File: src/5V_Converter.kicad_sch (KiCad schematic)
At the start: 13 parts, among them U3 TPS564257DRLR (12V-5V)

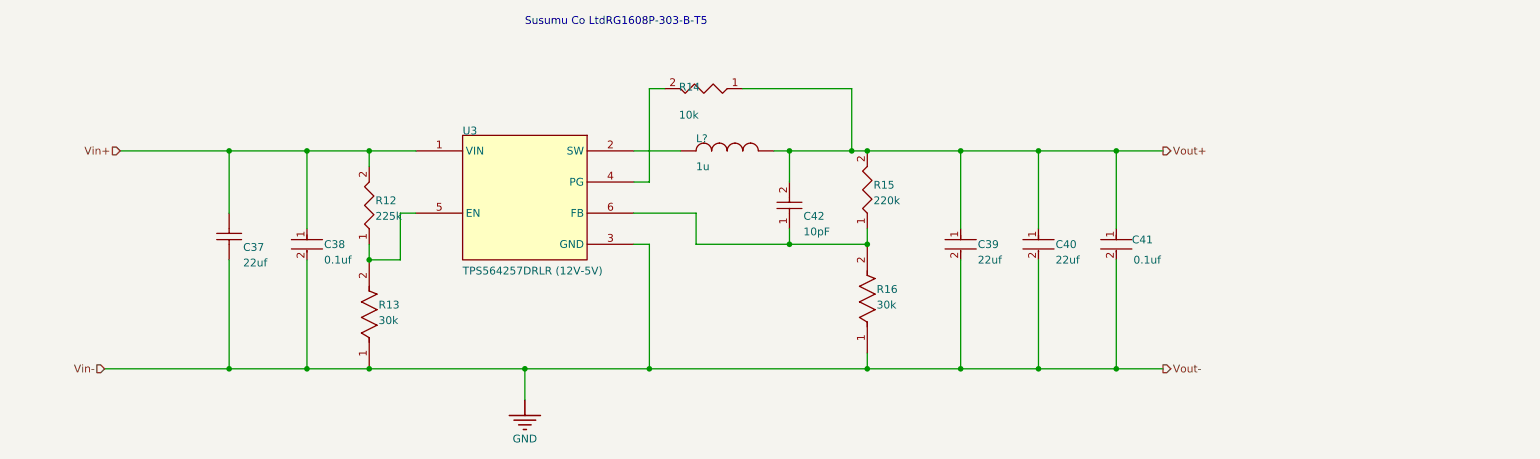
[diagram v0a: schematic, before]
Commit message: Updated majority of passive components to KiCad format
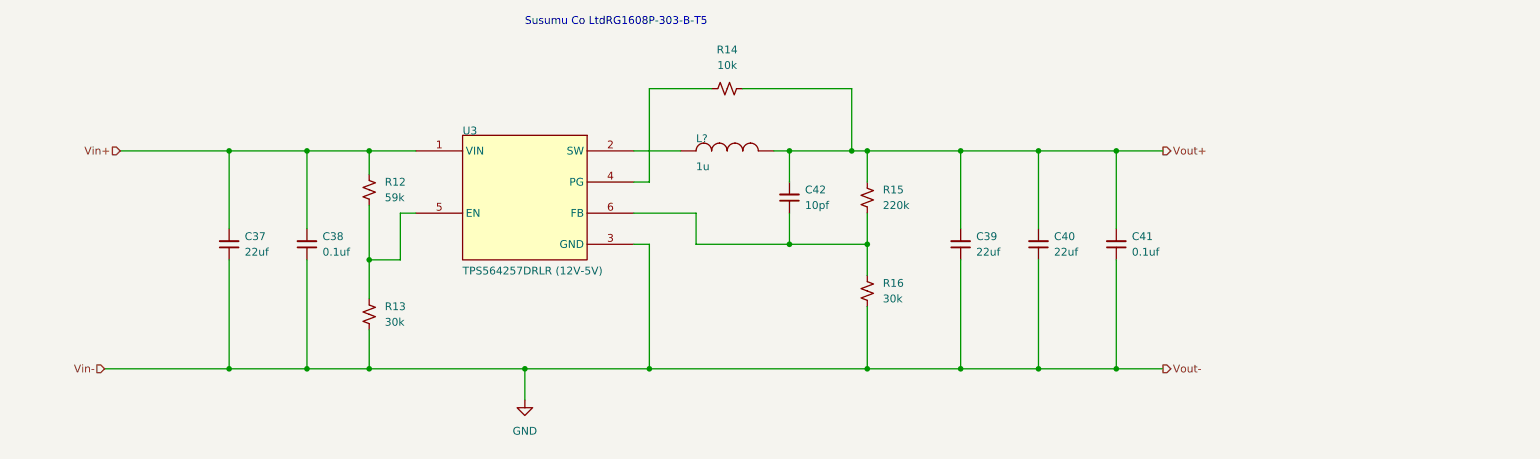
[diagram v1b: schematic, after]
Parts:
- removed C37: Capacitor, symbol Simulation Generic Components:Capacitor
- removed C38: 0.1uf, powerDristributionBoard-import-fps:FP-C0603C-CF-MFG, symbol Altium Content Vault:b4654b650e69147ec39a6b967a45e02
- removed C39, C40: 22uf, powerDristributionBoard-import-fps:FP-GRM21B-0_2-e0_2_0_7-IPC_C, symbol Altium Content Vault:b4654b650e69147ec39a6b967a45e02
- removed C41: 0.1uf, powerDristributionBoard-import-fps:FP-CGA3E-0_3-0_1-IPC_A, symbol Altium Content Vault:b4654b650e69147ec39a6b967a45e02
- removed C42: Capacitor 10 pF +/- 0.25 pF 50 V 0402, powerDristributionBoard-import-fps:CAPC1005X55X30LL05T10, symbol Autonomous Vehicle Lab:CAP-NP-2
- removed R12, R14, R15: 120R3J, powerDristributionBoard-import-fps:RESC0603(1608)_L, symbol Autonomous Vehicle Lab:120R3J
- removed R13, R16: 30k, powerDristributionBoard-import-fps:FP-RG1608-IPC_C, symbol Altium Content Vault:1029c3af85768c4190bb7ad29bc67b5
- added C37, C39, C40: 22uf, Capacitor_SMD:C_0805_2012Metric, symbol Device:C_Small
- added C38, C41: 0.1uf, Capacitor_SMD:C_0603_1608Metric, symbol Device:C_Small
- added C42: 10pf, Capacitor_SMD:C_0402_1005Metric, symbol Device:C_Small
- added R12: 59k, Resistor_SMD:R_0603_1608Metric, symbol Device:R_Small_US
- added R13, R16: 30k, Resistor_SMD:R_0603_1608Metric, symbol Device:R_Small_US
- added R14: 10k, Resistor_SMD:R_0603_1608Metric, symbol Device:R_Small_US
- added R15: 220k, Resistor_SMD:R_0603_1608Metric, symbol Device:R_Small_US
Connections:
- net GND: now also C37.1, C38.1, C39.1, C40.1, C41.1, R13.1, R16.1
- net Vin+: now also C37.2, C38.2, R12.2
- net Vout+: now also C39.2, C40.2, C41.2, C42.2, R14.2, R15.2
- net at U3.4 (PG): now also R14.1
- net at U3.5 (EN): now also R12.1, R13.2
- net at U3.6 (FB): now also C42.1, R15.1, R16.2

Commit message: Updated all passive components to KiCad version
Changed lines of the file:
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@@
 	(text "Susumu Co LtdRG1608P-303-B-T5"
 		(exclude_from_sim no)
-		(at 101.6 71.12 0)
+		(at 68.58 78.74 0)
 		(effects
 			(font

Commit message: Tweaked a lot stuff
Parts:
- gave numbers to parts that had none: 1
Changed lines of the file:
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@@
 		(instances
 			(project "powerDristributionBoard"
-				(path "/d5fc2ae9-f21d-48b0-bd61-912ade1f672f/f7fc7c23-3a4e-412b-b14d-71f85b15285a"
+				(path "/501e9f3f-9bfa-47dd-b56d-5fd6974f0d03/f7fc7c23-3a4e-412b-b14d-71f85b15285a"
 					(reference "R16")
 					(unit 1)
@@
 		(instances
 			(project "powerDristributionBoard"
-				(path "/d5fc2ae9-f21d-48b0-bd61-912ade1f672f/f7fc7c23-3a4e-412b-b14d-71f85b15285a"
+				(path "/501e9f3f-9bfa-47dd-b56d-5fd6974f0d03/f7fc7c23-3a4e-412b-b14d-71f85b15285a"
 					(reference "C37")
 					(unit 1)
@@
 		(instances
 			(project "powerDristributionBoard"
-				(path "/d5fc2ae9-f21d-48b0-bd61-912ade1f672f/f7fc7c23-3a4e-412b-b14d-71f85b15285a"
+				(path "/501e9f3f-9bfa-47dd-b56d-5fd6974f0d03/f7fc7c23-3a4e-412b-b14d-71f85b15285a"
 					(reference "#PWR016")
 					(unit 1)
@@
 		(instances
 			(project "powerDristributionBoard"
-				(path "/d5fc2ae9-f21d-48b0-bd61-912ade1f672f/f7fc7c23-3a4e-412b-b14d-71f85b15285a"
+				(path "/501e9f3f-9bfa-47dd-b56d-5fd6974f0d03/f7fc7c23-3a4e-412b-b14d-71f85b15285a"
 					(reference "U3")
 					(unit 1)
@@
 		(instances
 			(project "powerDristributionBoard"
-				(path "/d5fc2ae9-f21d-48b0-bd61-912ade1f672f/f7fc7c23-3a4e-412b-b14d-71f85b15285a"
+				(path "/501e9f3f-9bfa-47dd-b56d-5fd6974f0d03/f7fc7c23-3a4e-412b-b14d-71f85b15285a"
 					(reference "C41")
 					(unit 1)
@@
 		(instances
 			(project "powerDristributionBoard"
-				(path "/d5fc2ae9-f21d-48b0-bd61-912ade1f672f/f7fc7c23-3a4e-412b-b14d-71f85b15285a"
+				(path "/501e9f3f-9bfa-47dd-b56d-5fd6974f0d03/f7fc7c23-3a4e-412b-b14d-71f85b15285a"
 					(reference "R14")
 					(unit 1)
@@
 		(instances
 			(project "powerDristributionBoard"
-				(path "/d5fc2ae9-f21d-48b0-bd61-912ade1f672f/f7fc7c23-3a4e-412b-b14d-71f85b15285a"
+				(path "/501e9f3f-9bfa-47dd-b56d-5fd6974f0d03/f7fc7c23-3a4e-412b-b14d-71f85b15285a"
 					(reference "C40")
 					(unit 1)
@@
 		(instances
 			(project "powerDristributionBoard"
-				(path "/d5fc2ae9-f21d-48b0-bd61-912ade1f672f/f7fc7c23-3a4e-412b-b14d-71f85b15285a"
+				(path "/501e9f3f-9bfa-47dd-b56d-5fd6974f0d03/f7fc7c23-3a4e-412b-b14d-71f85b15285a"
 					(reference "C42")
 					(unit 1)
@@
 		(instances
 			(project "powerDristributionBoard"
-				(path "/d5fc2ae9-f21d-48b0-bd61-912ade1f672f/f7fc7c23-3a4e-412b-b14d-71f85b15285a"
+				(path "/501e9f3f-9bfa-47dd-b56d-5fd6974f0d03/f7fc7c23-3a4e-412b-b14d-71f85b15285a"
 					(reference "C39")
 					(unit 1)
@@
 		(instances
 			(project "powerDristributionBoard"
-				(path "/d5fc2ae9-f21d-48b0-bd61-912ade1f672f/f7fc7c23-3a4e-412b-b14d-71f85b15285a"
+				(path "/501e9f3f-9bfa-47dd-b56d-5fd6974f0d03/f7fc7c23-3a4e-412b-b14d-71f85b15285a"
 					(reference "R12")
 					(unit 1)
@@
 		(in_pos_files yes)
 		(dnp no)
-		(property "Reference" "L?"
+		(property "Reference" "L2"
 			(at 129.54 90.17 0)
 			(show_name no)
@@
 		(instances
 			(project "powerDristributionBoard"
-				(path "/d5fc2ae9-f21d-48b0-bd61-912ade1f672f/f7fc7c23-3a4e-412b-b14d-71f85b15285a"
-					(reference "L?")
+				(path "/501e9f3f-9bfa-47dd-b56d-5fd6974f0d03/f7fc7c23-3a4e-412b-b14d-71f85b15285a"
+					(reference "L2")
 					(unit 1)
 				)
@@
 		(instances
 			(project "powerDristributionBoard"
-				(path "/d5fc2ae9-f21d-48b0-bd61-912ade1f672f/f7fc7c23-3a4e-412b-b14d-71f85b15285a"
+				(path "/501e9f3f-9bfa-47dd-b56d-5fd6974f0d03/f7fc7c23-3a4e-412b-b14d-71f85b15285a"
 					(reference "R15")
 					(unit 1)
@@
 		(instances
 			(project "powerDristributionBoard"
-				(path "/d5fc2ae9-f21d-48b0-bd61-912ade1f672f/f7fc7c23-3a4e-412b-b14d-71f85b15285a"
+				(path "/501e9f3f-9bfa-47dd-b56d-5fd6974f0d03/f7fc7c23-3a4e-412b-b14d-71f85b15285a"
 					(reference "R13")
 					(unit 1)
@@
 		(instances
 			(project "powerDristributionBoard"
-				(path "/d5fc2ae9-f21d-48b0-bd61-912ade1f672f/f7fc7c23-3a4e-412b-b14d-71f85b15285a"
+				(path "/501e9f3f-9bfa-47dd-b56d-5fd6974f0d03/f7fc7c23-3a4e-412b-b14d-71f85b15285a"
 					(reference "C38")
 					(unit 1)

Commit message: Pushing remaining schematic files
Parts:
- removed L2: Inductor, symbol Simulation Generic Components:Inductor
- added L2: 1uH, symbol Device:L
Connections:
- net Vout+: now also L2.2
- net at U3.2 (SW): now also L2.1
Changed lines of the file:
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@@
 	(generator_version "10.0")
 	(paper "A")
+	(rectangle
+		(start 127 83.82)
+		(end 142.24 95.25)
+		(stroke
+			(width 0)
+			(type solid)
+			(color 255 7 0 1)
+		)
+		(fill
+			(type none)
+		)
+	)
 	(text "Susumu Co LtdRG1608P-303-B-T5"
 		(exclude_from_sim no)
@@
 	(wire
 		(pts
-			(xy 127 91.44) (xy 119.38 91.44)
+			(xy 119.38 91.44) (xy 130.81 91.44)
 		)
 		(stroke
@@
 	(wire
 		(pts
-			(xy 144.78 91.44) (xy 142.24 91.44)
-		)
-		(stroke
-			(width 0)
-			(type default)
-		)
-	)
-	(wire
-		(pts
 			(xy 154.94 91.44) (xy 144.78 91.44)
 		)
@@
 		(pts
 			(xy 144.78 96.52) (xy 144.78 91.44)
+		)
+		(stroke
+			(width 0)
+			(type default)
+		)
+	)
+	(wire
+		(pts
+			(xy 138.43 91.44) (xy 144.78 91.44)
 		)
 		(stroke
@@
 	)
 	(symbol
-		(lib_id "Simulation Generic Components:Inductor")
-		(at 127 91.44 0)
+		(lib_id "Device:L")
+		(at 134.62 91.44 90)
 		(unit 1)
 		(body_style 1)
@@
 		(in_pos_files yes)
 		(dnp no)
+		(fields_autoplaced yes)
 		(property "Reference" "L2"
-			(at 129.54 90.17 0)
-			(show_name no)
-			(do_not_autoplace no)
-			(effects
-				(font
-					(size 1.27 1.27)
-				)
-				(justify left bottom)
-			)
-		)
-		(property "Value" "Inductor"
-			(at 129.54 94.742 0)
-			(hide yes)
-			(show_name no)
-			(do_not_autoplace no)
-			(effects
-				(font
-					(size 1.27 1.27)
-				)
-				(justify left bottom)
+			(at 134.62 86.36 90)
+			(show_name no)
+			(do_not_autoplace no)
+			(effects
+				(font
+					(size 1.27 1.27)
+				)
+			)
+		)
+		(property "Value" "1uH"
+			(at 134.62 88.9 90)
+			(show_name no)
+			(do_not_autoplace no)
+			(effects
+				(font
+					(size 1.27 1.27)
+				)
 			)
 		)
 		(property "Footprint" ""
-			(at 127 91.44 0)
+			(at 134.62 91.44 0)
 			(hide yes)
 			(show_name no)
@@
 		)
 		(property "Datasheet" ""
-			(at 127 91.44 0)
+			(at 134.62 91.44 0)
 			(hide yes)
 			(show_name no)
@@
 		)
 		(property "Description" "Inductor"
-			(at 127 91.44 0)
-			(hide yes)
-			(show_name no)
-			(do_not_autoplace no)
-			(effects
-				(font
-					(size 1.27 1.27)
-				)
-			)
-		)
-		(property "SIMULATIONGENERICCOMPONENT" "True"
-			(at 129.54 97.282 0)
-			(hide yes)
-			(show_name no)
-			(do_not_autoplace no)
-			(effects
-				(font
-					(size 1.27 1.27)
-				)
-				(justify left bottom)
-			)
-		)
-		(property "DTEMP" ""
-			(at 142.748 92.202 0)
-			(hide yes)
-			(show_name no)
-			(do_not_autoplace no)
-			(effects
-				(font
-					(size 1.27 1.27)
-				)
-				(justify left bottom)
-			)
-		)
-		(property "T_REL_LOCAL" ""
-			(at 142.748 92.202 0)
-			(hide yes)
-			(show_name no)
-			(do_not_autoplace no)
-			(effects
-				(font
-					(size 1.27 1.27)
-				)
-				(justify left bottom)
-			)
-		)
-		(property "INITIAL CURRENT" ""
-			(at 142.748 92.202 0)
-			(hide yes)
-			(show_name no)
-			(do_not_autoplace no)
-			(effects
-				(font
-					(size 1.27 1.27)
-				)
-				(justify left bottom)
-			)
-		)
-		(property "CPAR" ""
-			(at 142.748 92.202 0)
-			(hide yes)
-			(show_name no)
-			(do_not_autoplace no)
-			(effects
-				(font
-					(size 1.27 1.27)
-				)
-				(justify left bottom)
-			)
-		)
-		(property "M" ""
-			(at 142.748 92.202 0)
-			(hide yes)
-			(show_name no)
-			(do_not_autoplace no)
-			(effects
-				(font
-					(size 1.27 1.27)
-				)
-				(justify left bottom)
-			)
-		)
-		(property "RPAR" ""
-			(at 142.748 92.202 0)
-			(hide yes)
-			(show_name no)
-			(do_not_autoplace no)
-			(effects
-				(font
-					(size 1.27 1.27)
-				)
-				(justify left bottom)
-			)
-		)
-		(property "RSER" ""
-			(at 142.748 92.202 0)
-			(hide yes)
-			(show_name no)
-			(do_not_autoplace no)
-			(effects
-				(font
-					(size 1.27 1.27)
-				)
-				(justify left bottom)
-			)
-		)
-		(property "TC1" ""
-			(at 142.748 92.202 0)
-			(hide yes)
-			(show_name no)
-			(do_not_autoplace no)
-			(effects
-				(font
-					(size 1.27 1.27)
-				)
-				(justify left bottom)
-			)
-		)
-		(property "TC2" ""
-			(at 142.748 92.202 0)
-			(hide yes)
-			(show_name no)
-			(do_not_autoplace no)
-			(effects
-				(font
-					(size 1.27 1.27)
-				)
-				(justify left bottom)
-			)
-		)
-		(property "TEMP" ""
-			(at 142.748 92.202 0)
-			(hide yes)
-			(show_name no)
-			(do_not_autoplace no)
-			(effects
-				(font
-					(size 1.27 1.27)
-				)
-				(justify left bottom)
-			)
-		)
-		(property "ALTIUM_VALUE" "1u"
-			(at 129.54 94.742 0)
-			(show_name no)
-			(do_not_autoplace no)
-			(effects
-				(font
-					(size 1.27 1.27)
-				)
-				(justify left bottom)
-			)
+			(at 134.62 91.44 0)
+			(hide yes)
+			(show_name no)
+			(do_not_autoplace no)
+			(effects
+				(font
+					(size 1.27 1.27)
+				)
+			)
+		)
+		(pin "2"
 		)
 		(pin "1"
 		)
-		(pin "2"
-		)
 		(instances

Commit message: Added many footprints
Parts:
- U3: footprint (none) -> PowerPCB_Footprints:TPS564257DRLR
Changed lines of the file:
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@@
 			)
 		)
-		(property "Footprint" ""
+		(property "Footprint" "PowerPCB_Footprints:TPS564257DRLR"
 			(at 76.2 106.68 0)
 			(hide yes)

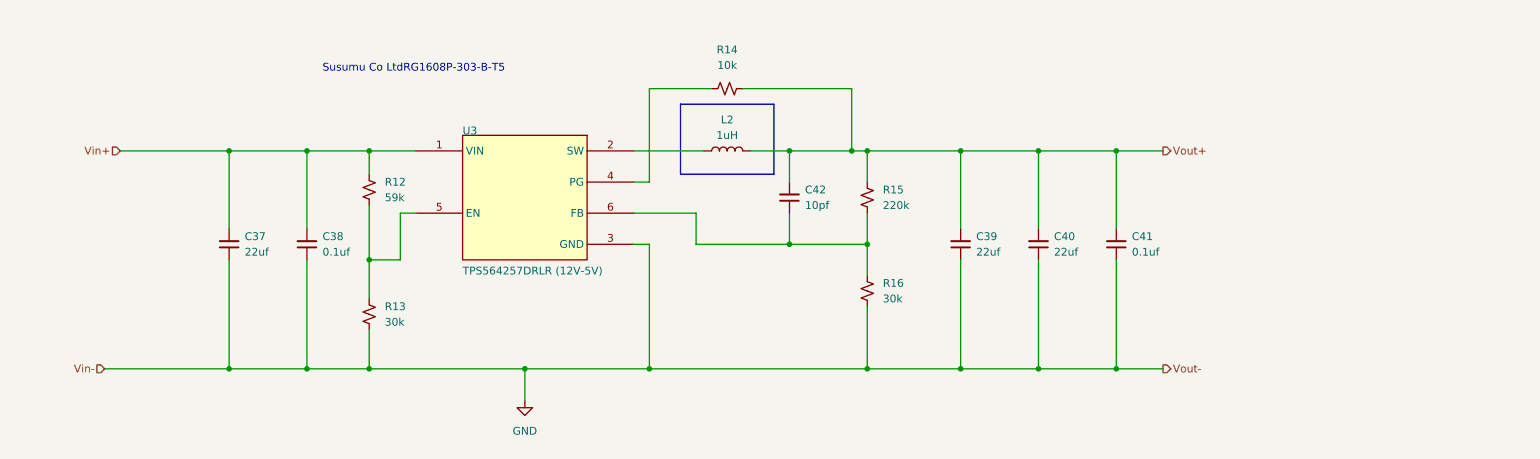
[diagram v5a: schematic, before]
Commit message: Redesigned 5V regulator and edited libraries
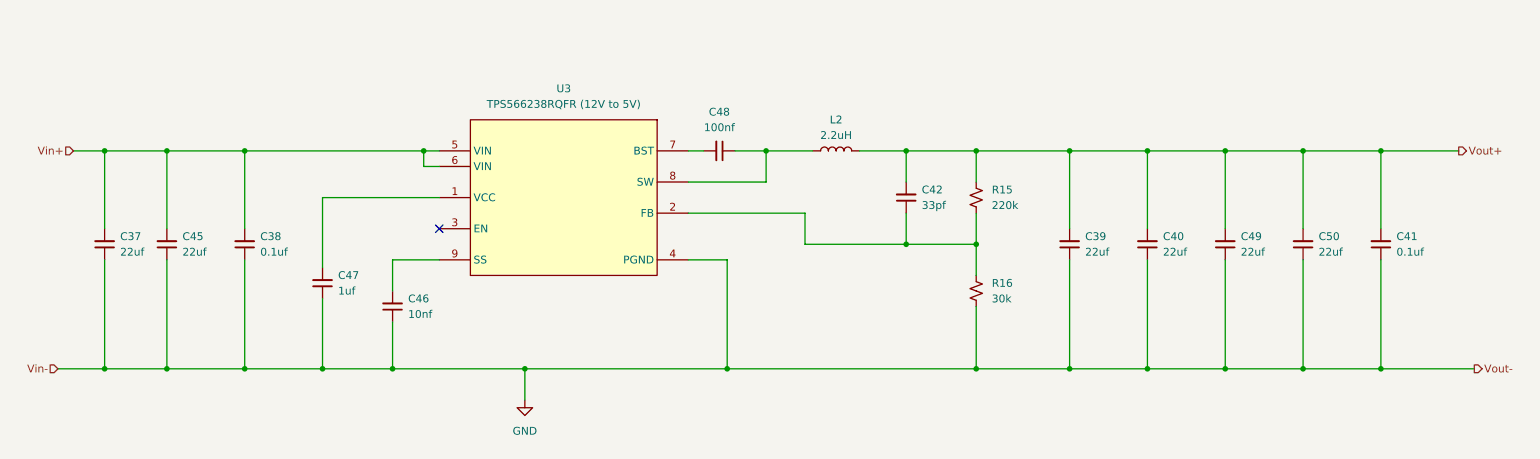
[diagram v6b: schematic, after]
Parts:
- removed R12: 59k, Resistor_SMD:R_0603_1608Metric, symbol Device:R_Small_US
- removed R13: 30k, Resistor_SMD:R_0603_1608Metric, symbol Device:R_Small_US
- removed R14: 10k, Resistor_SMD:R_0603_1608Metric, symbol Device:R_Small_US
- removed U3: TPS564257DRLR (12V-5V), PowerPCB_Footprints:TPS564257DRLR, symbol Schlib1:TPS564257DRLR (12V-5V)
- added C45, C49, C50: 22uf, Capacitor_SMD:C_0805_2012Metric, symbol Device:C_Small
- added C46: 10nf, Capacitor_SMD:C_0402_1005Metric, symbol Device:C_Small
- added C47: 1uf, Capacitor_SMD:C_0603_1608Metric, symbol Device:C_Small
- added C48: 100nf, Capacitor_SMD:C_0402_1005Metric, symbol Device:C_Small
- added U3: TPS566238RQFR (12V to 5V), PowerPCB_Footprints:TPS566238RQFR, symbol PowerPCB_Symbols:TPS566238RQFR
- C42: value 10pf -> 33pf; footprint Capacitor_SMD:C_0402_1005Metric -> Capacitor_SMD:C_0201_0603Metric
- L2: value 1uH -> 2.2uH; footprint (none) -> PowerPCB_Footprints:DR125-2R2-R
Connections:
- net GND: now also C45.1, C46.1, C47.1, C49.1, C50.1, U3.4 (PGND)
- net Vin+: now also C45.2, U3.5 (VIN), U3.6 (VIN)
- net Vout+: now also C49.2, C50.2
- net at C42.1, R15.1, R16.2: now also U3.2 (FB)
- net at L2.1: now also C48.1, U3.8 (SW)
- new net: C48.2, U3.7 (BST)
- new net: C46.2, U3.9 (SS)
- new net: C47.2, U3.1 (VCC)
- no-connect marks 0 -> 1
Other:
- note removed: "Susumu Co LtdRG1608P-303-B-T5"
- moved on the sheet: C37, C38, C39, C40, C41, C42, L2, R15, R16

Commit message: Finalized schematic
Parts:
- U3: value TPS566238RQFR (12V to 5V) -> TPS566238RQFR
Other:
- moved on the sheet: C37, C38, C39, C40, C41, C42, C45, C46, C47, C48, C49, C50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
